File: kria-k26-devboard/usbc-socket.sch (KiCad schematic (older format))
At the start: 8 parts, among them J10 USB4105-GF-A, Q11 DTC014TEBTL, Q15 PJA3441, U53 WE-TVS-82400152, U56 WE-TVS-82400152

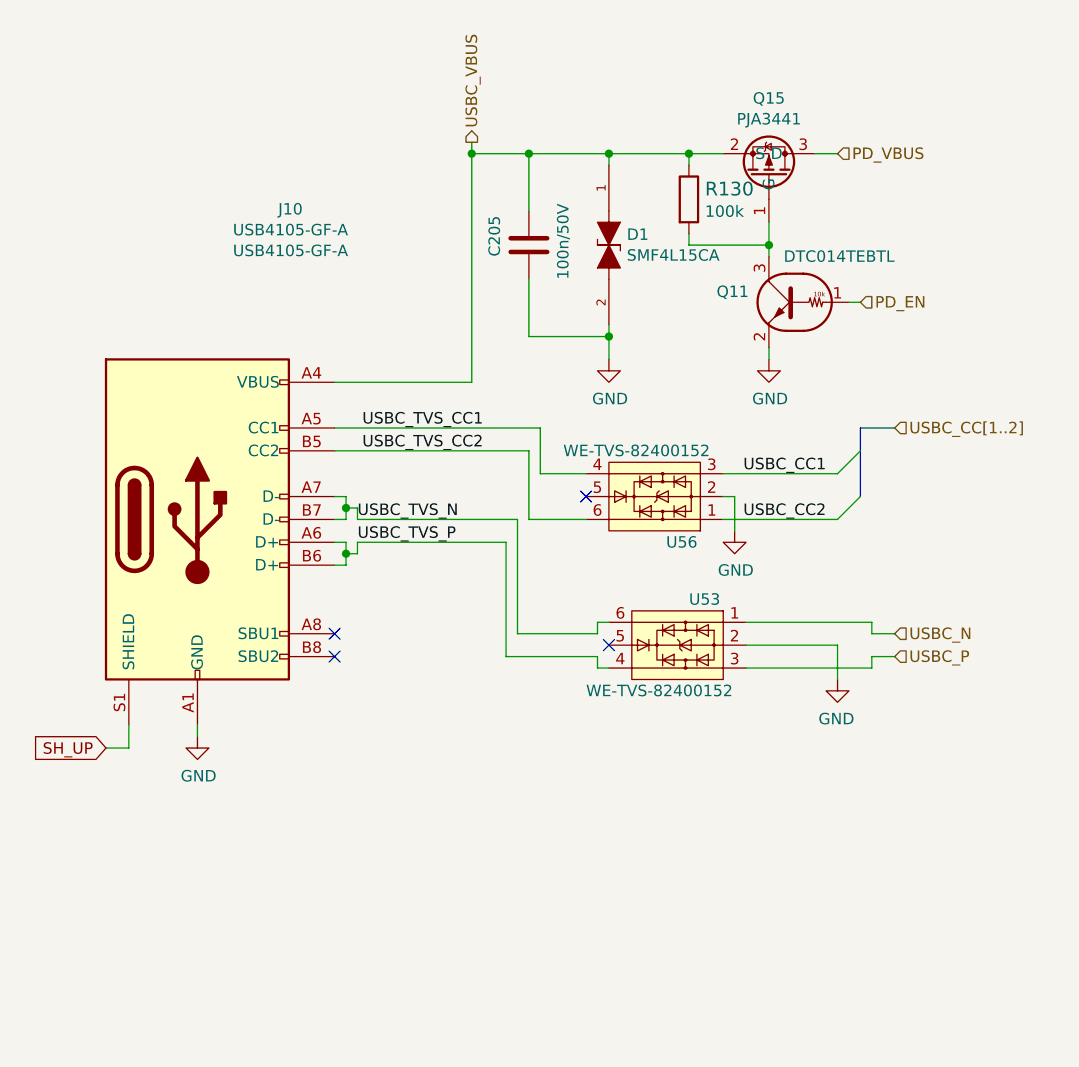
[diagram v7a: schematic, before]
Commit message: Fixed missing USB - M2 connection, finishing touches of PCB
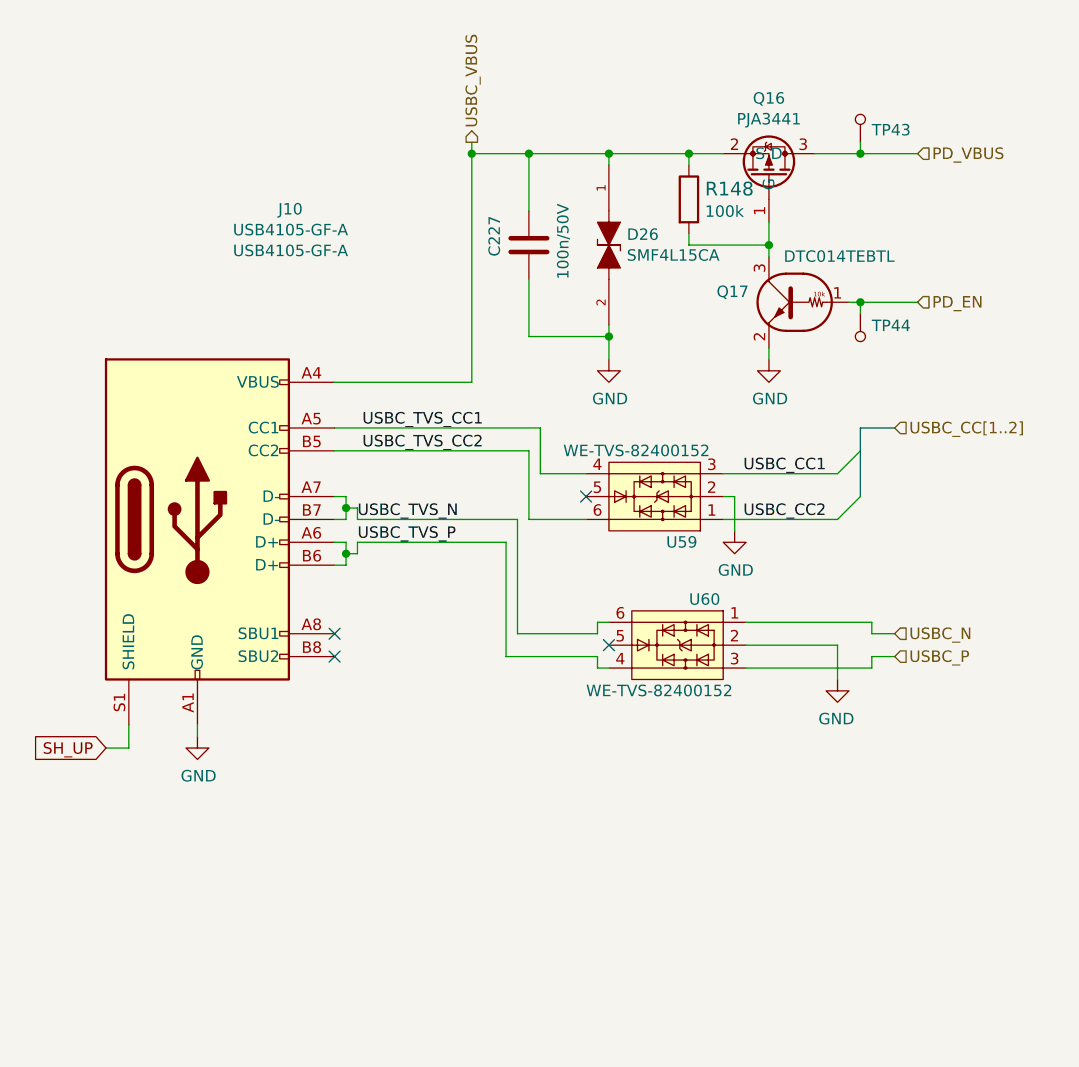
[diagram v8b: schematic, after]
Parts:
- added TP43, TP44: TP_SMD_0_75MM, antmicro-footprints:Testpoint_smd_0_75mm, symbol antmicroTestPoints:TP_SMD_0_75MM
- renumbered C205 to C227, D1 to D26, Q15 to Q16, Q11 to Q17, R130 to R148, U56 to U59, U53 to U60
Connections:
- net PD_EN: now also TP44.1
- net PD_VBUS: now also TP43.1
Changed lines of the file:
@@
 P 5600 3150
 AR Path="/63C44BC2/62AA368C" Ref="#PWR?"  Part="1"
-AR Path="/63C44BC2/62A9ECDC/62AA368C" Ref="#PWR0376"  Part="1"
-F 0 "#PWR0376" H 5600 2900 50  0001 C CNN
+AR Path="/63C44BC2/62A9ECDC/62AA368C" Ref="#PWR0400"  Part="1"
+F 0 "#PWR0400" H 5600 2900 50  0001 C CNN
 F 1 "GND" H 5605 2977 50  0000 C CNN
 F 2 "" H 5600 3150 50  0001 C CNN
@@
 P 5250 2650
 AR Path="/63C44BC2/62AA369D" Ref="C?"  Part="1"
-AR Path="/63C44BC2/62A9ECDC/62AA369D" Ref="C205"  Part="1"
-F 0 "C205" V 5100 2600 50  0000 L CNN
+AR Path="/63C44BC2/62A9ECDC/62AA369D" Ref="C227"  Part="1"
+F 0 "C227" V 5100 2600 50  0000 L CNN
 F 1 "C_100n_0402_50V" H 5250 2650 50  0001 C CNN
 F 2 "antmicro-footprints:0402-cap" H 5250 2650 50  0001 C CNN
@@
 Connection ~ 5250 2250
 $Comp
-L antmicroTransistorsFETsMOSFETsSingle:PJA3441 Q15
+L antmicroTransistorsFETsMOSFETsSingle:PJA3441 Q16
 U 1 1 661B0E3A
 P 6050 2300
-F 0 "Q15" V 6342 2550 50  0000 C CNN
+F 0 "Q16" V 6342 2550 50  0000 C CNN
 F 1 "PJA3441" V 6251 2550 50  0000 C CNN
 F 2 "antmicro-footprints:SOT-23-3" H 6050 2300 50  0001 C CNN
@@
 	5000 2250 5000 2200
 Connection ~ 5000 2250
-Text HLabel 6600 2250 2    50   Input ~ 0
+Text HLabel 6950 2250 2    50   Input ~ 0
 PD_VBUS
 Wire Wire Line
-	6500 2250 6600 2250
-$Comp
-L antmicroResistors0402:R_100k_0402 R130
+	6500 2250 6700 2250
+$Comp
+L antmicroResistors0402:R_100k_0402 R148
 U 1 1 661C93B4
 P 5950 2450
-F 0 "R130" V 5905 2520 60  0000 L CNN
+F 0 "R148" V 5905 2520 60  0000 L CNN
 F 1 "R_100k_0402" H 5950 2300 60  0001 C CNN
 F 2 "antmicro-footprints:0402-res" H 6150 2650 60  0001 L CNN
@@
 Wire Wire Line
 	6300 2650 6300 2550
-Text HLabel 6700 2900 2    50   Input ~ 0
+Text HLabel 6950 2900 2    50   Input ~ 0
 PD_EN
 Wire Wire Line
-	6700 2900 6650 2900
+	6950 2900 6700 2900
 Wire Wire Line
 	6300 2700 6300 2650
@@
 P 6300 3150
 AR Path="/63C44BC2/661D24DA" Ref="#PWR?"  Part="1"
-AR Path="/63C44BC2/62A9ECDC/661D24DA" Ref="#PWR0378"  Part="1"
-F 0 "#PWR0378" H 6300 2900 50  0001 C CNN
+AR Path="/63C44BC2/62A9ECDC/661D24DA" Ref="#PWR0402"  Part="1"
+F 0 "#PWR0402" H 6300 2900 50  0001 C CNN
 F 1 "GND" H 6305 2977 50  0000 C CNN
 F 2 "" H 6300 3150 50  0001 C CNN
@@
 USBC_CC1
 $Comp
-L antmicroTransistorsBipolarSingle:DTC014TEBTL Q11
+L antmicroTransistorsBipolarSingle:DTC014TEBTL Q17
 U 1 1 631791E8
 P 6400 2900
-F 0 "Q11" H 6588 2946 50  0000 L CNN
+F 0 "Q17" H 6588 2946 50  0000 L CNN
 F 1 "DTC014TEBTL" H 5950 3100 50  0000 L CNN
 F 2 "antmicro-footprints:SOT-416" H 6600 2600 50  0001 L CNN
@@
 P 5900 4400
 AR Path="/625B0244/62E99410" Ref="U?"  Part="1"
-AR Path="/63C44BC2/62A9ECDC/62E99410" Ref="U53"  Part="1"
-F 0 "U53" H 5850 4600 50  0000 R CNN
+AR Path="/63C44BC2/62A9ECDC/62E99410" Ref="U60"  Part="1"
+F 0 "U60" H 5850 4600 50  0000 R CNN
 F 1 "WE-TVS-82400152" H 6300 4200 50  0000 R CNN
 F 2 "antmicro-footprints:SOT-563" H 5900 4200 50  0001 C CNN
@@
 P 6600 4550
 AR Path="/63C44BC2/63812C2B" Ref="#PWR?"  Part="1"
-AR Path="/63C44BC2/62A9ECDC/63812C2B" Ref="#PWR0375"  Part="1"
-F 0 "#PWR0375" H 6600 4300 50  0001 C CNN
+AR Path="/63C44BC2/62A9ECDC/63812C2B" Ref="#PWR0403"  Part="1"
+F 0 "#PWR0403" H 6600 4300 50  0001 C CNN
 F 1 "GND" H 6605 4377 50  0000 C CNN
 F 2 "" H 6600 4550 50  0001 C CNN
@@
 P 5800 3750
 AR Path="/625B0244/6383DAA4" Ref="U?"  Part="1"
-AR Path="/63C44BC2/62A9ECDC/6383DAA4" Ref="U56"  Part="1"
-F 0 "U56" H 5750 3950 50  0000 R CNN
+AR Path="/63C44BC2/62A9ECDC/6383DAA4" Ref="U59"  Part="1"
+F 0 "U59" H 5750 3950 50  0000 R CNN
 F 1 "WE-TVS-82400152" H 6200 3550 50  0000 R CNN
 F 2 "antmicro-footprints:SOT-563" H 5800 3550 50  0001 C CNN
@@
 P 6150 3900
 AR Path="/63C44BC2/6386B45F" Ref="#PWR?"  Part="1"
-AR Path="/63C44BC2/62A9ECDC/6386B45F" Ref="#PWR0377"  Part="1"
-F 0 "#PWR0377" H 6150 3650 50  0001 C CNN
+AR Path="/63C44BC2/62A9ECDC/6386B45F" Ref="#PWR0401"  Part="1"
+F 0 "#PWR0401" H 6150 3650 50  0001 C CNN
 F 1 "GND" H 6155 3727 50  0000 C CNN
 F 2 "" H 6150 3900 50  0001 C CNN
@@
 	5200 4350 5550 4350
 $Comp
-L antmicroTVSDiodes:SMF4L15CA D1
+L antmicroTVSDiodes:SMF4L15CA D26
 U 1 1 626860F1
 P 5600 2650
-F 0 "D1" V 5554 2728 50  0000 L CNN
+F 0 "D26" V 5554 2728 50  0000 L CNN
 F 1 "SMF4L15CA" V 5645 2728 50  0000 L CNN
 F 2 "antmicro-footprints:SOD-123FL" H 5600 2650 50  0001 C CNN
@@
 AR Path="/63CADD16/629B8553" Ref="#PWR?"  Part="1"
 AR Path="/625B0244/629B8553" Ref="#PWR?"  Part="1"
-AR Path="/63C44BC2/62A9ECDC/629B8553" Ref="#PWR0418"  Part="1"
-F 0 "#PWR0418" H 3800 4550 50  0001 C CNN
+AR Path="/63C44BC2/62A9ECDC/629B8553" Ref="#PWR0399"  Part="1"
+F 0 "#PWR0399" H 3800 4550 50  0001 C CNN
 F 1 "GND" H 3805 4627 50  0000 C CNN
 F 2 "" H 3800 4800 50  0001 C CNN
@@
 AR Path="/63C44BC2/62AA367B" Ref="J?"  Part="1"
 AR Path="/63C44BC2/62A9ECDC/62AA367B" Ref="J10"  Part="1"
-AR Path="/62AA367B" Ref="J10"  Part="1"
+AR Path="/62AA367B" Ref="J?"  Part="1"
 F 0 "J10" H 4207 5207 50  0000 C CNN
 F 1 "USB4105-GF-A" H 4207 5116 50  0000 C CNN
@@
 Text GLabel 3400 4850 0    50   Input ~ 0
 SH_UP
+$Comp
+L antmicroTestPoints:TP_SMD_0_75MM TP43
+U 1 1 63201A0B
+P 6700 2100
+F 0 "TP43" H 6650 2147 50  0000 R CNN
+F 1 "TP_SMD_0_75MM" H 6700 2000 50  0001 C CNN
+F 2 "antmicro-footprints:Testpoint_smd_0_75mm" H 6900 2300 60  0001 L CNN
+F 3 "" H 6900 2400 60  0001 L CNN
+	1    6700 2100
+	-1   0    0    1
+$EndComp
+Wire Wire Line
+	6700 2250 6700 2200
+Connection ~ 6700 2250
+Wire Wire Line
+	6700 2250 6950 2250
+$Comp
+L antmicroTestPoints:TP_SMD_0_75MM TP44
+U 1 1 6320BA28
+P 6700 3050
+F 0 "TP44" H 6750 3097 50  0000 L CNN
+F 1 "TP_SMD_0_75MM" H 6700 2950 50  0001 C CNN
+F 2 "antmicro-footprints:Testpoint_smd_0_75mm" H 6900 3250 60  0001 L CNN
+F 3 "" H 6900 3350 60  0001 L CNN
+	1    6700 3050
+	1    0    0    -1
+$EndComp
+Wire Wire Line
+	6700 2950 6700 2900
+Connection ~ 6700 2900
+Wire Wire Line
+	6700 2900 6650 2900
 Wire Bus Line
 	6700 3450 6700 3750
